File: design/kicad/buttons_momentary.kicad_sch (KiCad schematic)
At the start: 18 parts, among them J2 Conn_01x02_Socket, J3 Conn_01x02_Socket, J4 Conn_01x02_Socket, J5 Conn_01x02_Socket, J6 Conn_01x02_Socket, J7 Conn_01x02_Socket

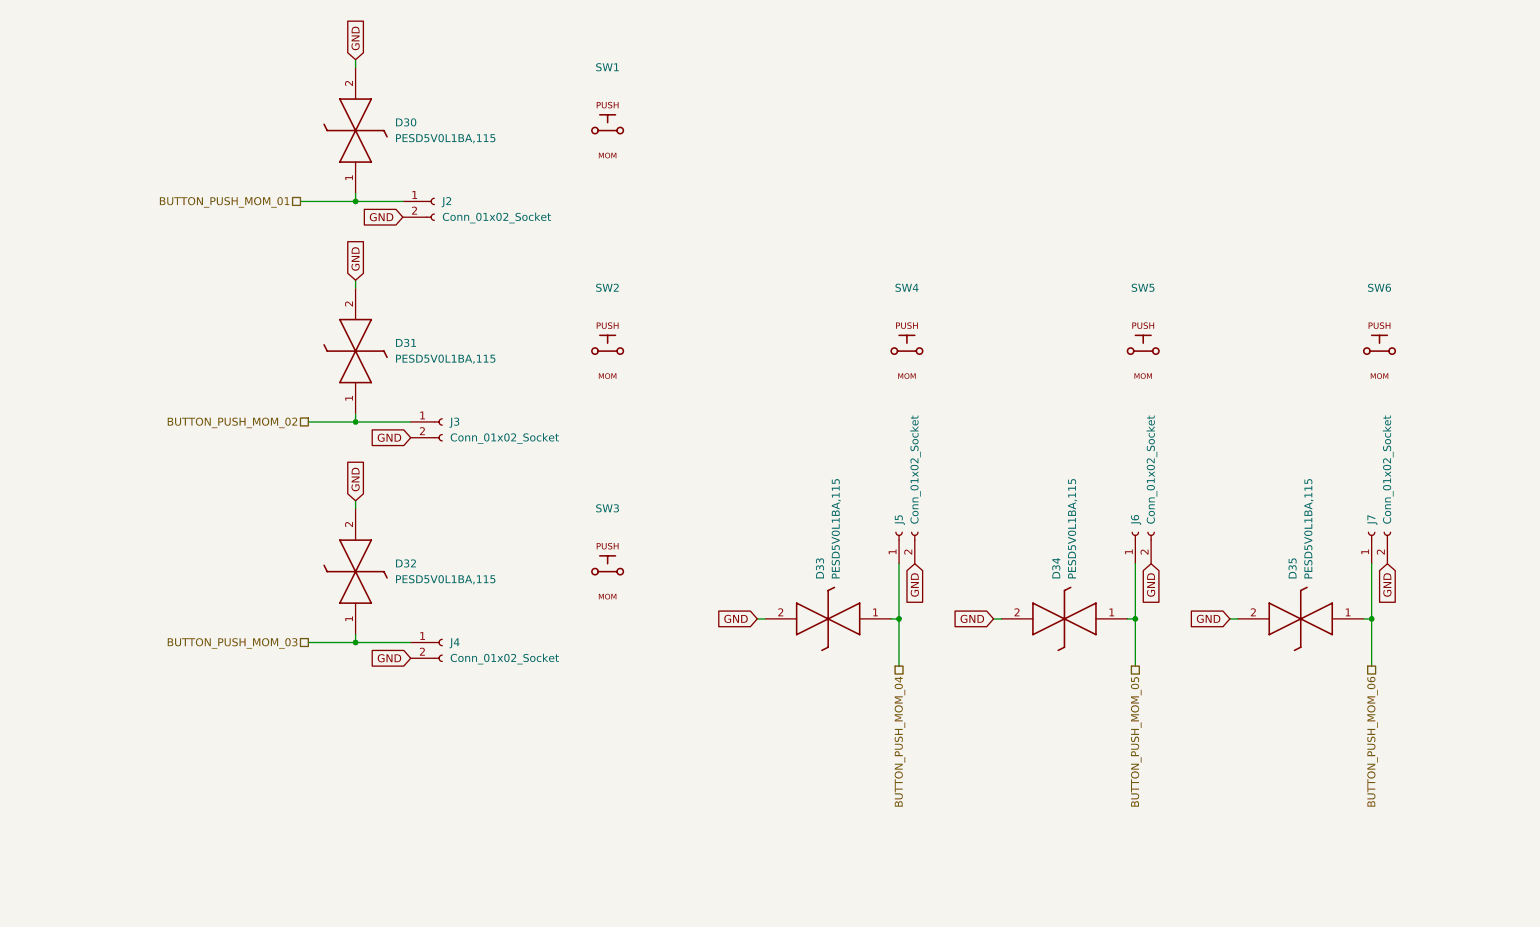
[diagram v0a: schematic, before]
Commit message: Update kicad binary files
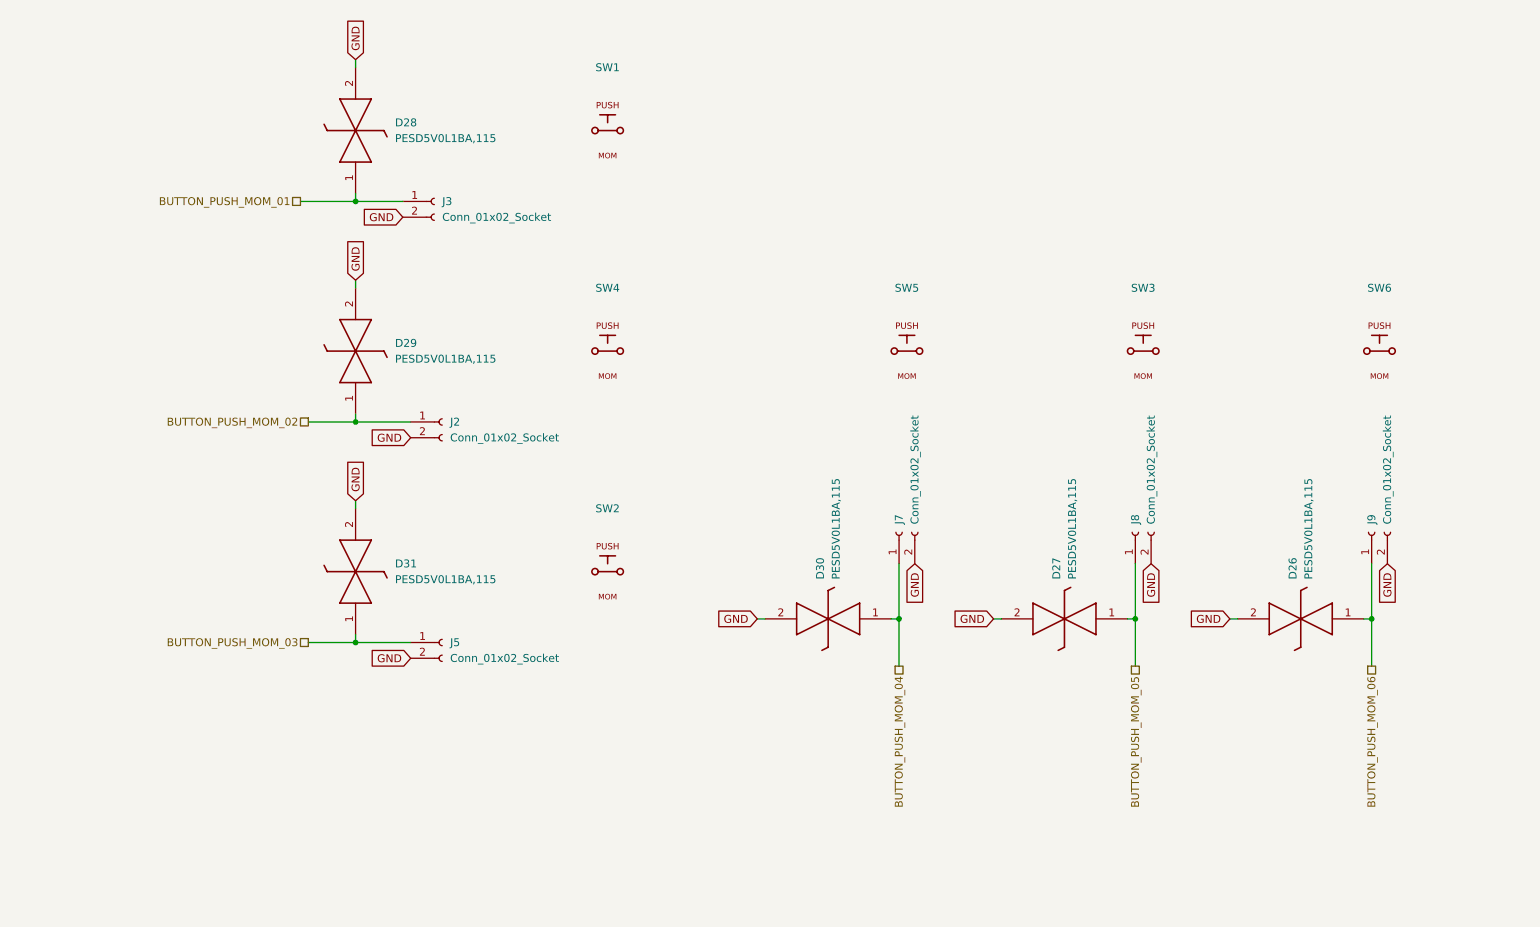
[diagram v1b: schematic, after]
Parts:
- D26: renamed from D35; LCSC (none) -> C85380
- D27: renamed from D34; LCSC (none) -> C85380
- D28: renamed from D30; LCSC (none) -> C85380
- D29: renamed from D31; LCSC (none) -> C85380
- D30: renamed from D33; LCSC (none) -> C85380
- D31: renamed from D32; LCSC (none) -> C85380
- J2: renamed from J3; LCSC (none) -> C2908600
- J3: renamed from J2; LCSC (none) -> C2908600
- J5: renamed from J4; LCSC (none) -> C2908600
- J7: renamed from J5; LCSC (none) -> C2908600
- J8: renamed from J6; LCSC (none) -> C2908600
- J9: renamed from J7; LCSC (none) -> C2908600
- SW1, SW6: now left out of the parts list
- SW2: renamed from SW3; now left out of the parts list
- SW3: renamed from SW5; now left out of the parts list
- SW4: renamed from SW2; now left out of the parts list
- SW5: renamed from SW4; now left out of the parts list
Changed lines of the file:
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@@
 		(unit 1)
 		(exclude_from_sim no)
-		(in_bom yes)
+		(in_bom no)
 		(on_board yes)
 		(dnp no)
@@
 		(dnp no)
 		(fields_autoplaced yes)
-		(property "Reference" "J2"
+		(property "Reference" "J3"
 			(at 82.55 53.3399 0)
 			(effects
@@
 			)
 		)
+		(property "LCSC" "C2908600"
+			(at 82.55 53.3399 0)
+			(effects
+				(font
+					(size 1.27 1.27)
+				)
+				(hide yes)
+			)
+		)
 		(pin "2"
 		)
@@
 			(project ""
 				(path "/9e44e663-00d0-4f33-bf1f-c4ad78deb554/9031f441-b35d-4c72-b3de-1ac6f4fd634b"
-					(reference "J2")
+					(reference "J3")
 					(unit 1)
 				)
@@
 		(dnp no)
 		(fields_autoplaced yes)
-		(property "Reference" "D34"
+		(property "Reference" "D27"
 			(at 181.6099 114.3 90)
 			(effects
@@
 			)
 		)
+		(property "LCSC" "C85380"
+			(at 181.6099 114.3 0)
+			(effects
+				(font
+					(size 1.27 1.27)
+				)
+				(hide yes)
+			)
+		)
 		(pin "1"
 		)
@@
 			(project "midi_controller"
 				(path "/9e44e663-00d0-4f33-bf1f-c4ad78deb554/9031f441-b35d-4c72-b3de-1ac6f4fd634b"
-					(reference "D34")
+					(reference "D27")
 					(unit 1)
 				)
@@
 		(dnp no)
 		(fields_autoplaced yes)
-		(property "Reference" "D31"
+		(property "Reference" "D29"
 			(at 74.93 76.1999 90)
 			(effects
@@
 			)
 		)
+		(property "LCSC" "C85380"
+			(at 74.93 76.1999 0)
+			(effects
+				(font
+					(size 1.27 1.27)
+				)
+				(hide yes)
+			)
+		)
 		(pin "1"
 		)
@@
 			(project "midi_controller"
 				(path "/9e44e663-00d0-4f33-bf1f-c4ad78deb554/9031f441-b35d-4c72-b3de-1ac6f4fd634b"
-					(reference "D31")
+					(reference "D29")
 					(unit 1)
 				)
@@
 		(unit 1)
 		(exclude_from_sim no)
-		(in_bom yes)
-		(on_board yes)
-		(dnp no)
-		(property "Reference" "SW4"
+		(in_bom no)
+		(on_board yes)
+		(dnp no)
+		(property "Reference" "SW5"
 			(at 157.48 67.31 0)
 			(effects
@@
 			(project "midi_controller"
 				(path "/9e44e663-00d0-4f33-bf1f-c4ad78deb554/9031f441-b35d-4c72-b3de-1ac6f4fd634b"
-					(reference "SW4")
+					(reference "SW5")
 					(unit 1)
 				)
@@
 		(dnp no)
 		(fields_autoplaced yes)
-		(property "Reference" "J7"
+		(property "Reference" "J9"
 			(at 232.4099 105.41 0)
 			(effects
@@
 			)
 		)
+		(property "LCSC" "C2908600"
+			(at 232.4099 105.41 0)
+			(effects
+				(font
+					(size 1.27 1.27)
+				)
+				(hide yes)
+			)
+		)
 		(pin "2"
 		)
@@
 			(project "midi_controller"
 				(path "/9e44e663-00d0-4f33-bf1f-c4ad78deb554/9031f441-b35d-4c72-b3de-1ac6f4fd634b"
-					(reference "J7")
+					(reference "J9")
 					(unit 1)
 				)
@@
 		(unit 1)
 		(exclude_from_sim no)
-		(in_bom yes)
-		(on_board yes)
-		(dnp no)
-		(fields_autoplaced yes)
-		(property "Reference" "SW3"
+		(in_bom no)
+		(on_board yes)
+		(dnp no)
+		(fields_autoplaced yes)
+		(property "Reference" "SW2"
 			(at 109.22 102.87 0)
 			(effects
@@
 			(project "midi_controller"
 				(path "/9e44e663-00d0-4f33-bf1f-c4ad78deb554/9031f441-b35d-4c72-b3de-1ac6f4fd634b"
-					(reference "SW3")
+					(reference "SW2")
 					(unit 1)
 				)
@@
 		(dnp no)
 		(fields_autoplaced yes)
-		(property "Reference" "J5"
+		(property "Reference" "J7"
 			(at 156.2099 105.41 0)
 			(effects
@@
 			)
 		)
+		(property "LCSC" "C2908600"
+			(at 156.2099 105.41 0)
+			(effects
+				(font
+					(size 1.27 1.27)
+				)
+				(hide yes)
+			)
+		)
 		(pin "2"
 		)
@@
 			(project "midi_controller"
 				(path "/9e44e663-00d0-4f33-bf1f-c4ad78deb554/9031f441-b35d-4c72-b3de-1ac6f4fd634b"
-					(reference "J5")
+					(reference "J7")
 					(unit 1)
 				)
@@
 		(dnp no)
 		(fields_autoplaced yes)
-		(property "Reference" "J6"
+		(property "Reference" "J8"
 			(at 194.3099 105.41 0)
 			(effects
@@
 			)
 		)
+		(property "LCSC" "C2908600"
+			(at 194.3099 105.41 0)
+			(effects
+				(font
+					(size 1.27 1.27)
+				)
+				(hide yes)
+			)
+		)
 		(pin "2"
 		)
@@
 			(project "midi_controller"
 				(path "/9e44e663-00d0-4f33-bf1f-c4ad78deb554/9031f441-b35d-4c72-b3de-1ac6f4fd634b"
-					(reference "J6")
+					(reference "J8")
 					(unit 1)
 				)
@@
 		(dnp no)
 		(fields_autoplaced yes)
-		(property "Reference" "D30"
+		(property "Reference" "D28"
 			(at 74.93 40.6399 90)
 			(effects
@@
 			)
 		)
+		(property "LCSC" "C85380"
+			(at 74.93 40.6399 0)
+			(effects
+				(font
+					(size 1.27 1.27)
+				)
+				(hide yes)
+			)
+		)
 		(pin "1"
 		)
@@
 			(project "midi_controller"
 				(path "/9e44e663-00d0-4f33-bf1f-c4ad78deb554/9031f441-b35d-4c72-b3de-1ac6f4fd634b"
-					(reference "D30")
+					(reference "D28")
 					(unit 1)
 				)
@@
 		(dnp no)
 		(fields_autoplaced yes)
-		(property "Reference" "J3"
+		(property "Reference" "J2"
 			(at 83.82 88.8999 0)
 			(effects
@@
 			)
 		)
+		(property "LCSC" "C2908600"
+			(at 83.82 88.8999 0)
+			(effects
+				(font
+					(size 1.27 1.27)
+				)
+				(hide yes)
+			)
+		)
 		(pin "2"
 		)
@@
 			(project "midi_controller"
 				(path "/9e44e663-00d0-4f33-bf1f-c4ad78deb554/9031f441-b35d-4c72-b3de-1ac6f4fd634b"
-					(reference "J3")
+					(reference "J2")
 					(unit 1)
 				)
@@
 		(unit 1)
 		(exclude_from_sim no)
-		(in_bom yes)
+		(in_bom no)
 		(on_board yes)
 		(dnp no)
@@
 		(dnp no)
 		(fields_autoplaced yes)
-		(property "Reference" "D33"
+		(property "Reference" "D30"
 			(at 143.5099 114.3 90)
 			(effects
@@
 			)
 		)
+		(property "LCSC" "C85380"
+			(at 143.5099 114.3 0)
+			(effects
+				(font
+					(size 1.27 1.27)
+				)
+				(hide yes)
+			)
+		)
 		(pin "1"
 		)
@@
 			(project "midi_controller"
 				(path "/9e44e663-00d0-4f33-bf1f-c4ad78deb554/9031f441-b35d-4c72-b3de-1ac6f4fd634b"
-					(reference "D33")
+					(reference "D30")
 					(unit 1)
 				)
@@
 		(dnp no)
 		(fields_autoplaced yes)
-		(property "Reference" "J4"
+		(property "Reference" "J5"
 			(at 83.82 124.4599 0)
 			(effects
@@
 			)
 		)
+		(property "LCSC" "C2908600"
+			(at 83.82 124.4599 0)
+			(effects
+				(font
+					(size 1.27 1.27)
+				)
+				(hide yes)
+			)
+		)
 		(pin "2"
 		)
@@
 			(project "midi_controller"
 				(path "/9e44e663-00d0-4f33-bf1f-c4ad78deb554/9031f441-b35d-4c72-b3de-1ac6f4fd634b"
-					(reference "J4")
+					(reference "J5")
 					(unit 1)
 				)
@@
 		(unit 1)
 		(exclude_from_sim no)
-		(in_bom yes)
-		(on_board yes)
-		(dnp no)
-		(fields_autoplaced yes)
-		(property "Reference" "SW5"
+		(in_bom no)
+		(on_board yes)
+		(dnp no)
+		(fields_autoplaced yes)
+		(property "Reference" "SW3"
 			(at 195.58 67.31 0)
 			(effects
@@
 			(project "midi_controller"
 				(path "/9e44e663-00d0-4f33-bf1f-c4ad78deb554/9031f441-b35d-4c72-b3de-1ac6f4fd634b"
-					(reference "SW5")
+					(reference "SW3")
 					(unit 1)
 				)
@@
 		(dnp no)
 		(fields_autoplaced yes)
-		(property "Reference" "D35"
+		(property "Reference" "D26"
 			(at 219.7099 114.3 90)
 			(effects
@@
 			)
 		)
+		(property "LCSC" "C85380"
+			(at 219.7099 114.3 0)
+			(effects
+				(font
+					(size 1.27 1.27)
+				)
+				(hide yes)
+			)
+		)
 		(pin "1"
 		)
@@
 			(project "midi_controller"
 				(path "/9e44e663-00d0-4f33-bf1f-c4ad78deb554/9031f441-b35d-4c72-b3de-1ac6f4fd634b"
-					(reference "D35")
+					(reference "D26")
 					(unit 1)
 				)
@@
 		(unit 1)
 		(exclude_from_sim no)
-		(in_bom yes)
-		(on_board yes)
-		(dnp no)
-		(fields_autoplaced yes)
-		(property "Reference" "SW2"
+		(in_bom no)
+		(on_board yes)
+		(dnp no)
+		(fields_autoplaced yes)
+		(property "Reference" "SW4"
 			(at 109.22 67.31 0)
 			(effects
@@
 			(project "midi_controller"
 				(path "/9e44e663-00d0-4f33-bf1f-c4ad78deb554/9031f441-b35d-4c72-b3de-1ac6f4fd634b"
-					(reference "SW2")
+					(reference "SW4")
 					(unit 1)
 				)
@@
 		(dnp no)
 		(fields_autoplaced yes)
-		(property "Reference" "D32"
+		(property "Reference" "D31"
 			(at 74.93 111.7599 90)
 			(effects
@@
 			)
 		)
+		(property "LCSC" "C85380"
+			(at 74.93 111.7599 0)
+			(effects
+				(font
+					(size 1.27 1.27)
+				)
+				(hide yes)
+			)
+		)
 		(pin "1"
 		)
@@
 			(project "midi_controller"
 				(path "/9e44e663-00d0-4f33-bf1f-c4ad78deb554/9031f441-b35d-4c72-b3de-1ac6f4fd634b"
-					(reference "D32")
-					(unit 1)
-				)
+					(reference "D31")
+					(unit 1)
+				)

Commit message: Update kicad binary files
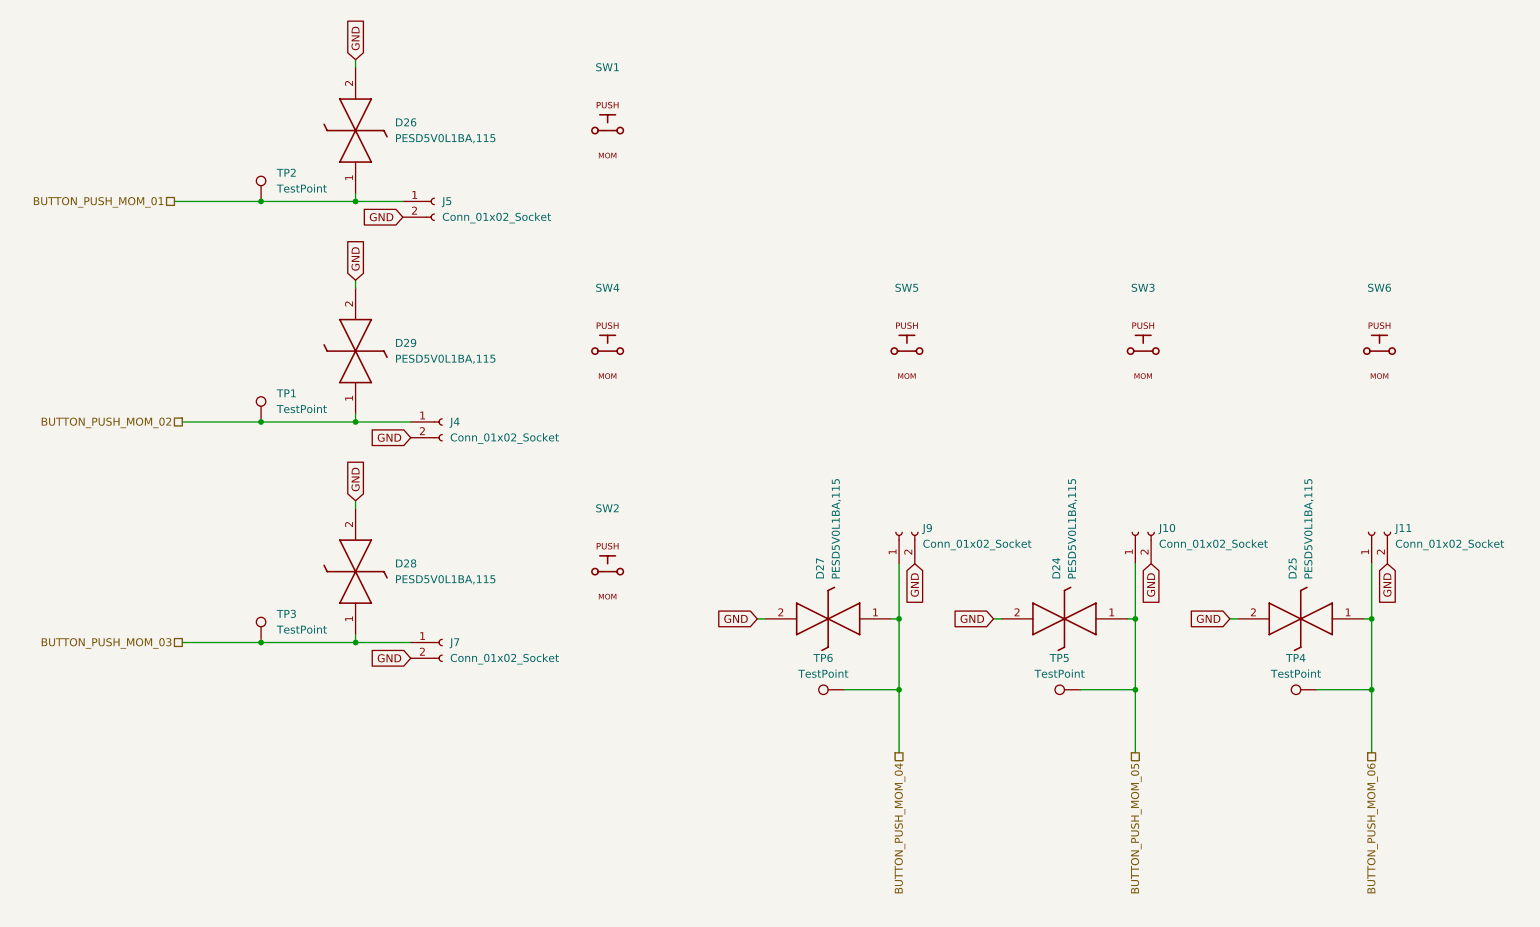
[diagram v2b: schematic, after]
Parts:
- added TP1, TP2, TP3, TP4, TP5, TP6: TestPoint, midi_controller:TestPoint_Pad_1.0x1.0mm, symbol midi_controller:TestPoint
- J10: renamed from J8; footprint Connector_JST:JST_XH_B2B-XH-A_1x02_P2.50mm_Vertical -> midi_controller:JST_XH_B2B-XH-A_1x02_P2.50mm_Vertical_JLC_Constraints; symbol Connector:Conn_01x02_Socket -> midi_controller:Conn_01x02_Socket
- J11: renamed from J9; footprint Connector_JST:JST_XH_B2B-XH-A_1x02_P2.50mm_Vertical -> midi_controller:JST_XH_B2B-XH-A_1x02_P2.50mm_Vertical_JLC_Constraints; symbol Connector:Conn_01x02_Socket -> midi_controller:Conn_01x02_Socket
- J4: renamed from J2; footprint Connector_JST:JST_XH_B2B-XH-A_1x02_P2.50mm_Vertical -> midi_controller:JST_XH_B2B-XH-A_1x02_P2.50mm_Vertical_JLC_Constraints; symbol Connector:Conn_01x02_Socket -> midi_controller:Conn_01x02_Socket
- J5: renamed from J3; footprint Connector_JST:JST_XH_B2B-XH-A_1x02_P2.50mm_Vertical -> midi_controller:JST_XH_B2B-XH-A_1x02_P2.50mm_Vertical_JLC_Constraints; symbol Connector:Conn_01x02_Socket -> midi_controller:Conn_01x02_Socket
- J7: renamed from J5; footprint Connector_JST:JST_XH_B2B-XH-A_1x02_P2.50mm_Vertical -> midi_controller:JST_XH_B2B-XH-A_1x02_P2.50mm_Vertical_JLC_Constraints; symbol Connector:Conn_01x02_Socket -> midi_controller:Conn_01x02_Socket
- J9: renamed from J7; footprint Connector_JST:JST_XH_B2B-XH-A_1x02_P2.50mm_Vertical -> midi_controller:JST_XH_B2B-XH-A_1x02_P2.50mm_Vertical_JLC_Constraints; symbol Connector:Conn_01x02_Socket -> midi_controller:Conn_01x02_Socket
- renumbered D27 to D24, D26 to D25, D28 to D26, D30 to D27, D31 to D28
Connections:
- net BUTTON_PUSH_MOM_01: now also TP2.1
- net BUTTON_PUSH_MOM_02: now also TP1.1
- net BUTTON_PUSH_MOM_03: now also TP3.1
- net BUTTON_PUSH_MOM_04: now also TP6.1
- net BUTTON_PUSH_MOM_05: now also TP5.1
- net BUTTON_PUSH_MOM_06: now also TP4.1
